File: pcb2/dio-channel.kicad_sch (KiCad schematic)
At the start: 7 parts, among them J1 Conn_01x03, SW1 SW_SPDT_MSM, U3 74hct08

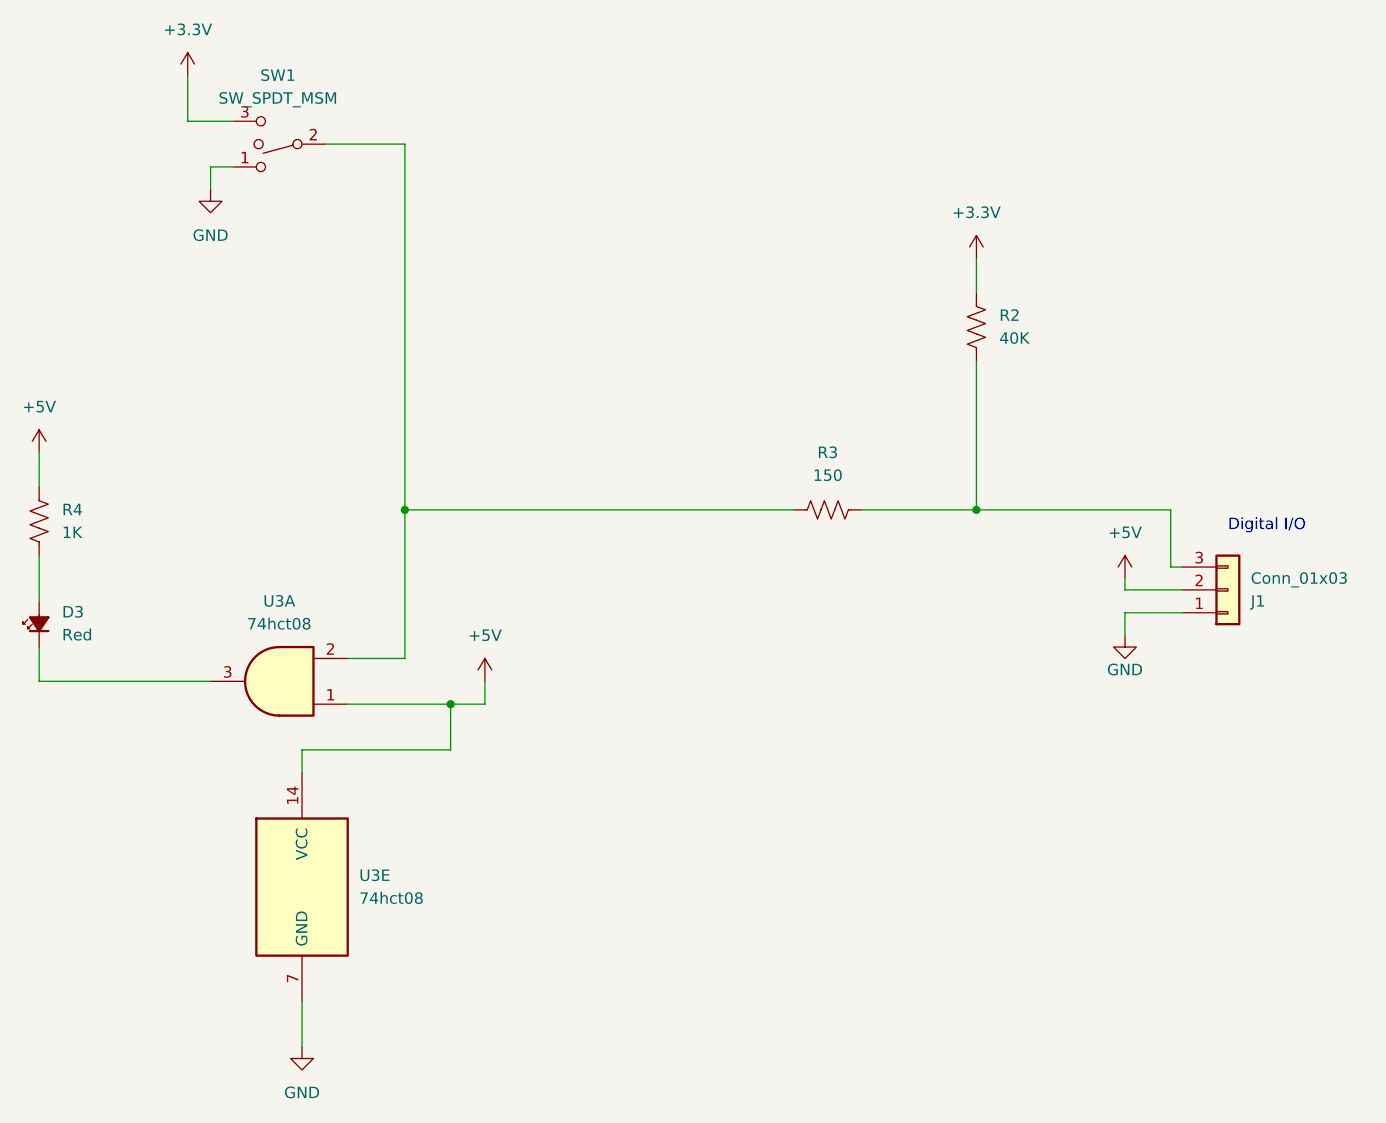
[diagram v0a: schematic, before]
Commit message: create fooprint for e-switch switch for SW1 etc get to a pretty good part placement, but want to try a variation
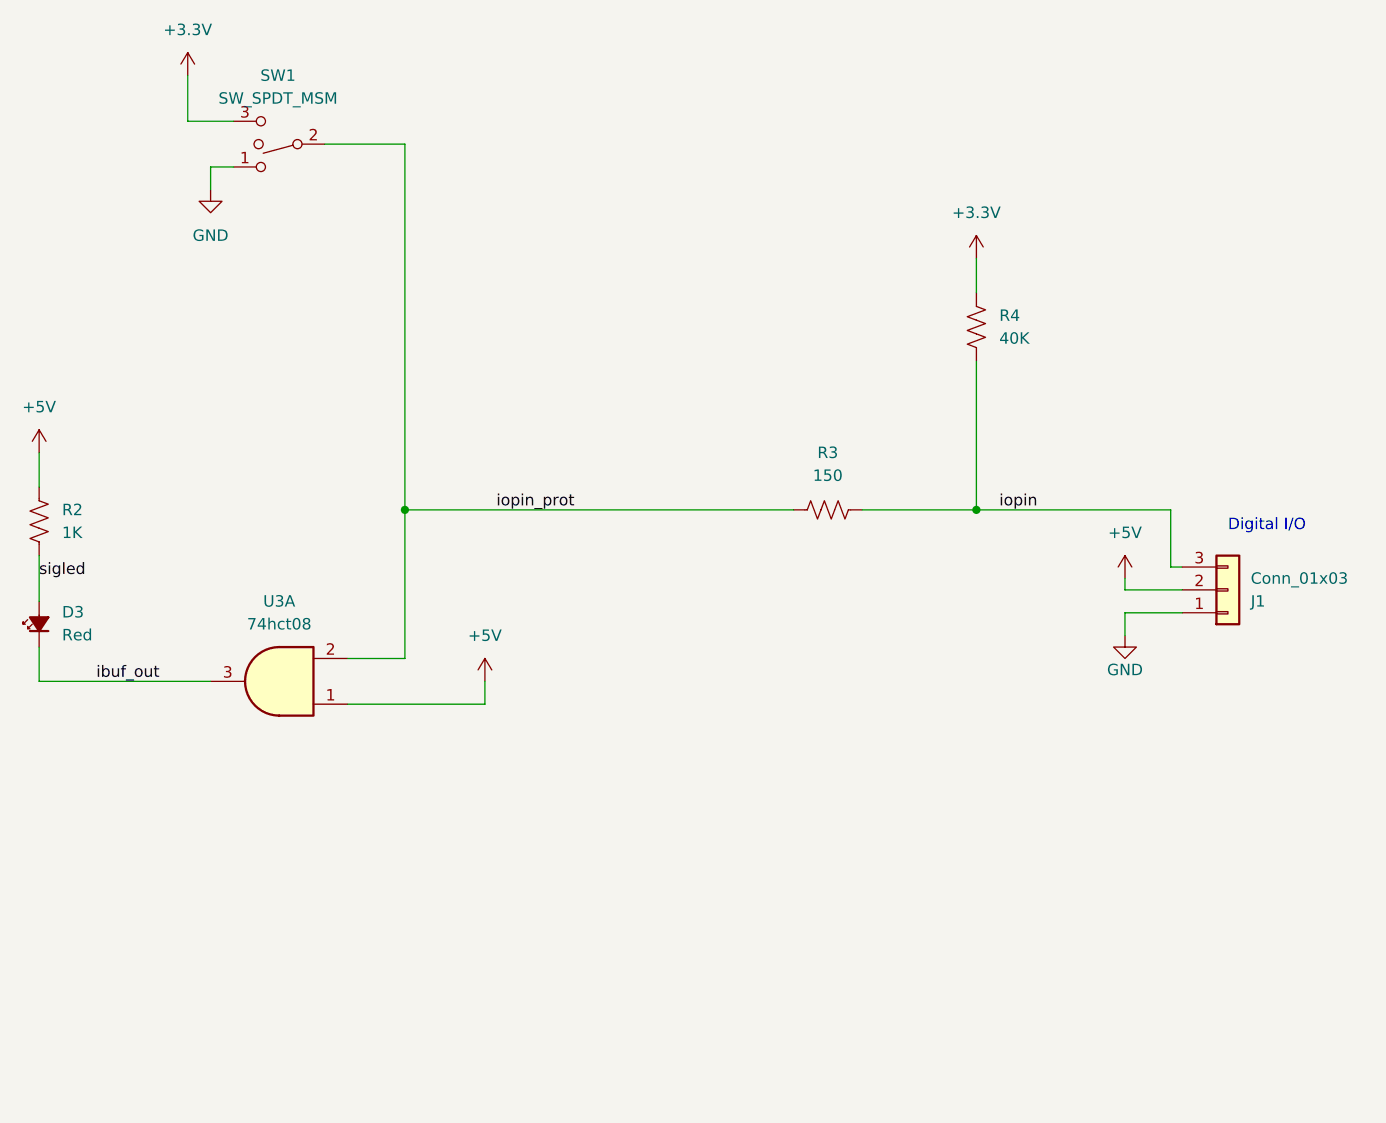
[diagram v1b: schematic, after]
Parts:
- removed unit 5 of U3
- D3: footprint (none) -> LED_THT:LED_D5.0mm
- J1: footprint (none) -> Connector_PinHeader_2.54mm:PinHeader_1x03_P2.54mm_Vertical
- R2: renamed from R4; footprint (none) -> Resistor_THT:R_Axial_DIN0207_L6.3mm_D2.5mm_P10.16mm_Horizontal
- R3: footprint (none) -> Resistor_THT:R_Axial_DIN0207_L6.3mm_D2.5mm_P10.16mm_Horizontal
- R4: renamed from R2; footprint (none) -> Resistor_THT:R_Axial_DIN0207_L6.3mm_D2.5mm_P10.16mm_Horizontal
- SW1: footprint (none) -> 0steve-footprints:SPDT-ESwitch-100SP3-M2
- U3: footprint (none) -> Package_DIP:DIP-14_W7.62mm_Socket
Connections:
- net iopin_prot: now reaches R3.1, SW1.2, U3.2
- net ibuf_out: now reaches D3.1 (K), U3.3
- net sigled: now reaches D3.2 (A), R2.2
- net iopin: now reaches J1.3 (Pin_3), R3.2, R4.2
